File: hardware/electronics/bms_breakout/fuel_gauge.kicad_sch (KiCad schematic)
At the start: 20 parts, among them Q4 BSS84, Q5 2N7002, Q6 2N7002, SW1 VAL, U3 BQ34Z100-R2

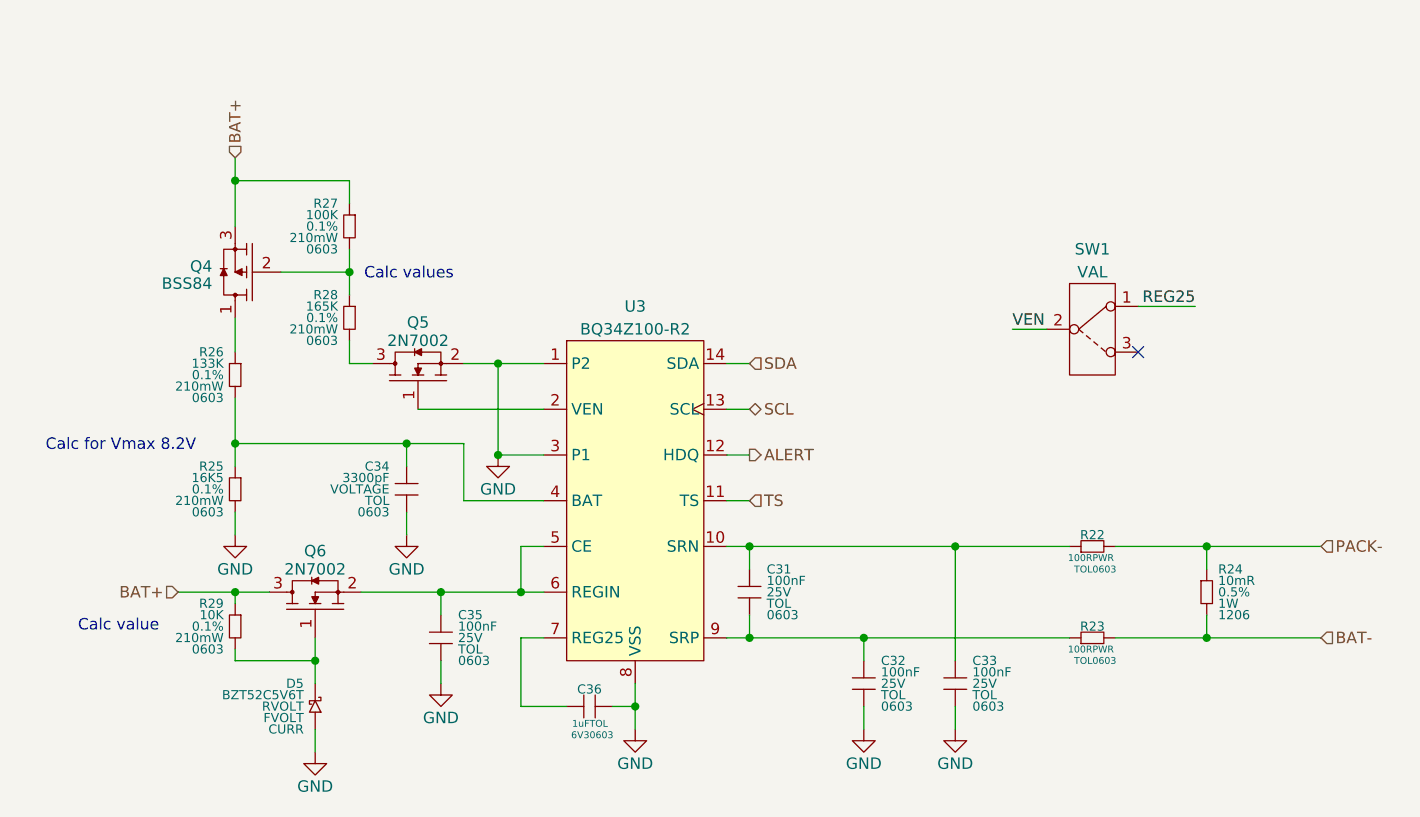
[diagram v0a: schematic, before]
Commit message: created child sheet for BQ34Z100
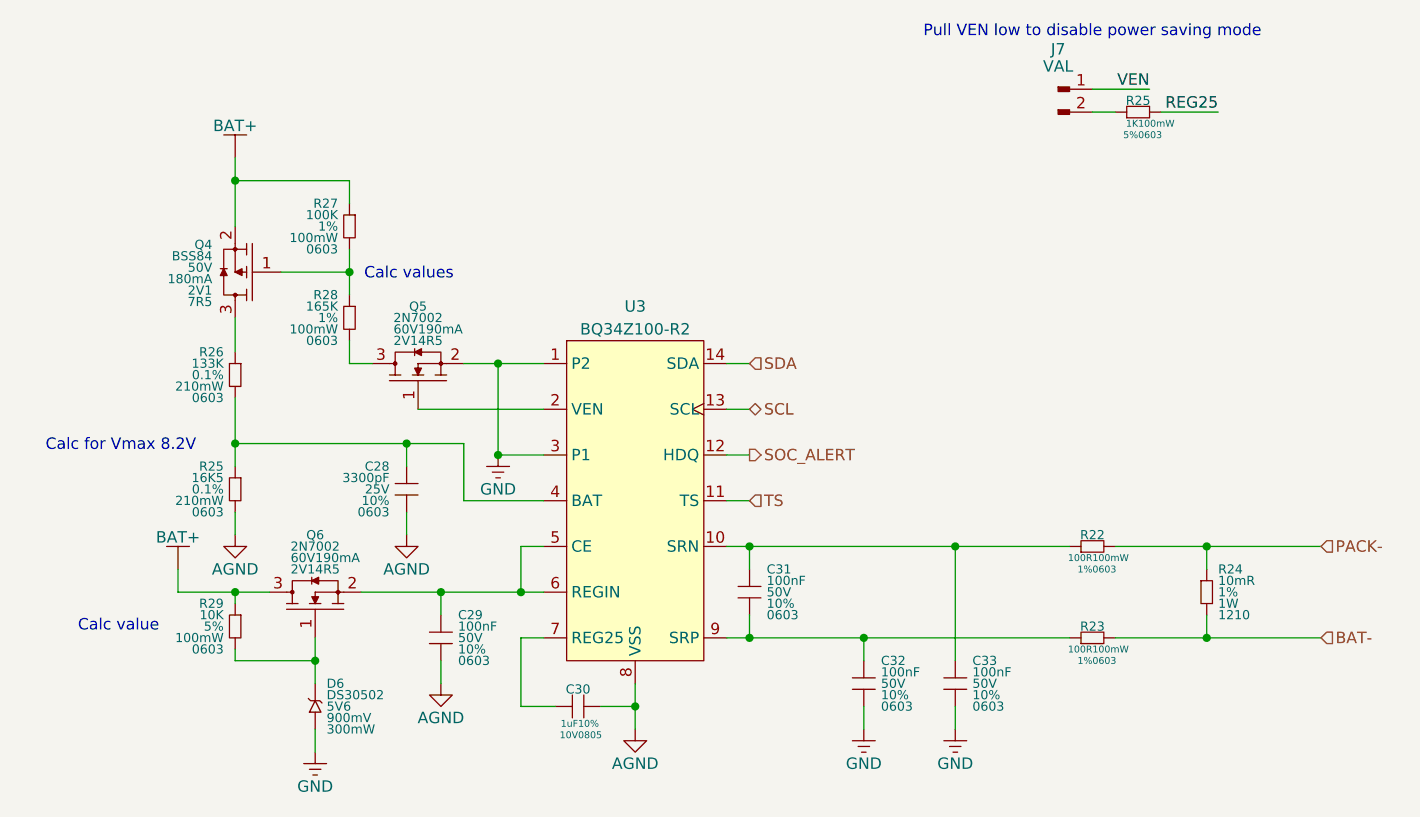
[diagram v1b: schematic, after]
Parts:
- removed C31, C32, C33, C35: 100nF, symbol DSE-Passives:C
- removed C34: 3300pF, symbol DSE-Passives:C
- removed C36: 1uF, symbol DSE-Passives:C_horizontal
- removed D5: BZT52C5V6T, symbol DSE-Passives:D_Schottky
- removed Q4: BSS84, symbol DSE-Transistors:PMOS_DGS
- removed Q5, Q6: 2N7002, symbol DSE-Transistors:NMOS_GSD
- removed R22, R23: 100R, symbol DSE-Passives:R_horizontal
- removed R27: 100K, symbol DSE-Passives:R
- removed R29: 10K, symbol DSE-Passives:R
- removed SW1: VAL, symbol DSE-Switches:SPDT
- added C28: 3300pF, symbol DS-Passives:C
- added C29, C31, C32, C33: 100nF, symbol DS-Passives:C
- added C30: 1uF, symbol DS-Passives:C_horizontal
- added D6: DS30502, symbol DS-Passives:D_Zener
- added J7: VAL, symbol DS-Connectors:Conn_01x02_Pin
- added Q4: BSS84, symbol DS-Transistors:PMOS_GSD
- added Q5, Q6: 2N7002, symbol DS-Transistors:NMOS_GSD
- added R22, R23: 100R, symbol DS-Passives:R_horizontal
- added R25: 1K, symbol DS-Passives:R_horizontal
- added R27: 100K, symbol DS-Passives:R
- added R29: 10K, symbol DS-Passives:R
- R24: DKPN 541-WSLP1206R0100DEACT-ND -> WSLF-.01CT-ND; MPN WSLP1206R0100DEA -> WSL2010R0100FEA18; Package 1206 -> 1210; Tolerance 0.5% -> 1%
- R28: DKPN 541-TNPW0603133KBEEACT-ND -> 541-165KHCT-ND; MPN TNPW0603133KBEEA -> CRCW0603165KFKEA; Power Rating 210mW -> 100mW; Tolerance 0.1% -> 1%
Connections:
- net BAT+: now also Q4.2, Q6.3, R27.1, R29.1
- net BAT-: now also R23.2
- net GND: now also C32.2, C33.2, D6.1, Q5.2; no longer R25.2, U3.8 (VSS)
- net PACK-: now also R22.2
- net REG25: now also R25.2
- net VEN: now also J7.1
- net at U3.10 (SRN): now also C31.1, C33.1, R22.1
- net at R28.1: now also Q4.1, R27.2
- net at R28.2: now also Q5.3
- net at U3.2 (VEN): now also Q5.1
- net at U3.5 (CE), U3.6 (REGIN): now also C29.1, Q6.2
- net at R25.1, R26.2, U3.4 (BAT): now also C28.1
- net at R26.1: now also Q4.3
- net at U3.9 (SRP): now also C31.2, C32.1, R23.1
- net at U3.7 (REG25): now also C30.1
- net ALERT renamed SOC_ALERT
- new net: D6.2, Q6.1, R29.2
- new net: J7.2, R25.1
- new net AGND: C28.2, C29.2, C30.2, R25.2, U3.8 (VSS)
- no-connect marks 1 -> 0
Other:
- note added: "Pull VEN low to disable power saving mode"
- title: (none) -> LiFePO4 State of Charge

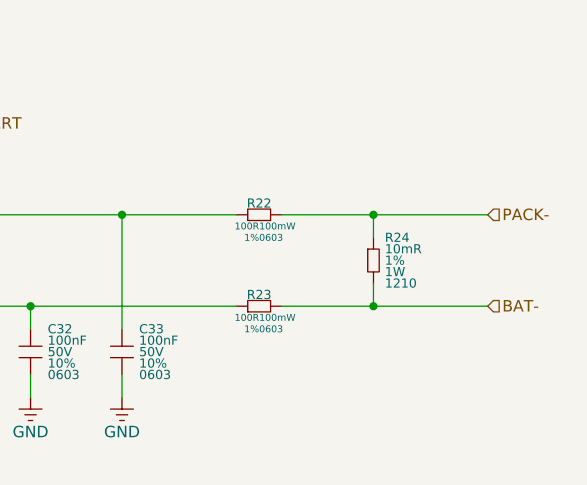
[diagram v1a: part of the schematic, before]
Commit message: added footprints for all resistors and capacitors
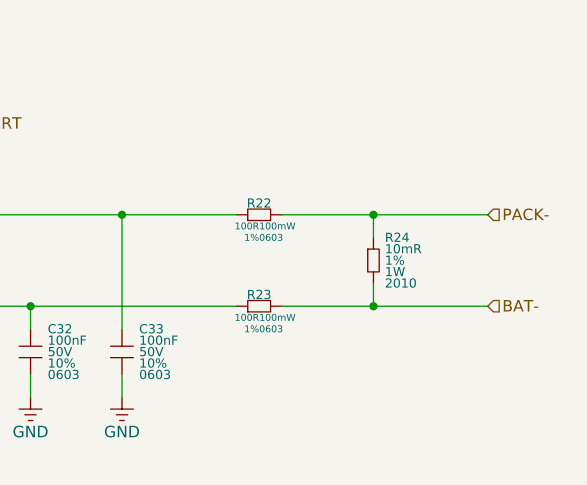
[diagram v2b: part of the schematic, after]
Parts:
- C28, C29, C31, C32, C33: footprint (none) -> DS-Capacitors-SMD:MLCC0603
- C30: footprint (none) -> DS-Capacitors-SMD:MLCC0805
- R22, R23, R25, R26, R27, R28, R29: footprint (none) -> DS-Resistors-SMD:CRCW0603
- R24: footprint (none) -> DS-Resistors-SMD:WSLHP2010; Package 1210 -> 2010
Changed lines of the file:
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@@
 			)
 		)
-		(property "Footprint" ""
+		(property "Footprint" "DS-Resistors-SMD:WSLHP2010"
 			(at 203.2 115.57 0)
 			(effects
@@
 			)
 		)
-		(property "Package" "1210"
+		(property "Package" "2010"
 			(at 204.47 120.65 0)
 			(do_not_autoplace yes)
@@
 			)
 		)
-		(property "Footprint" ""
+		(property "Footprint" "DS-Resistors-SMD:CRCW0603"
 			(at 107.95 85.09 0)
 			(effects
@@
 			)
 		)
-		(property "Footprint" ""
+		(property "Footprint" "DS-Capacitors-SMD:MLCC0603"
 			(at 165.1 126.365 0)
 			(effects
@@
 			)
 		)
-		(property "Footprint" ""
+		(property "Footprint" "DS-Resistors-SMD:CRCW0603"
 			(at 193.04 64.77 90)
 			(effects
@@
 			)
 		)
-		(property "Footprint" ""
+		(property "Footprint" "DS-Resistors-SMD:CRCW0603"
 			(at 107.95 74.93 0)
 			(effects
@@
 			)
 		)
-		(property "Footprint" ""
+		(property "Footprint" "DS-Resistors-SMD:CRCW0603"
 			(at 95.25 91.44 0)
 			(effects
@@
 			)
 		)
-		(property "Footprint" ""
+		(property "Footprint" "DS-Capacitors-SMD:MLCC0603"
 			(at 152.4 116.205 0)
 			(effects
@@
 			)
 		)
-		(property "Footprint" ""
+		(property "Footprint" "DS-Capacitors-SMD:MLCC0603"
 			(at 118.11 121.285 0)
 			(effects
@@
 			)
 		)
-		(property "Footprint" ""
+		(property "Footprint" "DS-Capacitors-SMD:MLCC0603"
 			(at 175.26 126.365 0)
 			(effects
@@
 			)
 		)
-		(property "Footprint" ""
+		(property "Footprint" "DS-Resistors-SMD:CRCW0603"
 			(at 187.96 113.03 90)
 			(effects
@@
 			)
 		)
-		(property "Footprint" ""
+		(property "Footprint" "DS-Capacitors-SMD:MLCC0603"
 			(at 114.3 104.775 0)
 			(effects
@@
 			)
 		)
-		(property "Footprint" ""
+		(property "Footprint" "DS-Resistors-SMD:CRCW0603"
 			(at 95.25 119.38 0)
 			(effects
@@
 			)
 		)
-		(property "Footprint" ""
+		(property "Footprint" "DS-Resistors-SMD:CRCW0603"
 			(at 187.96 123.19 90)
 			(effects
@@
 			)
 		)
-		(property "Footprint" ""
+		(property "Footprint" "DS-Capacitors-SMD:MLCC0805"
 			(at 133.35 136.525 0)
 			(effects
@@
 			)
 		)
-		(property "Footprint" ""
+		(property "Footprint" "DS-Resistors-SMD:CRCW0603"
 			(at 95.25 104.14 0)
 			(effects
